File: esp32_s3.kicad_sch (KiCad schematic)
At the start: 4 parts, among them J1 uart, J2 Conn_01x02, J4 i2c, U7 ESP32-S3-DEVKITC-1-N8R2

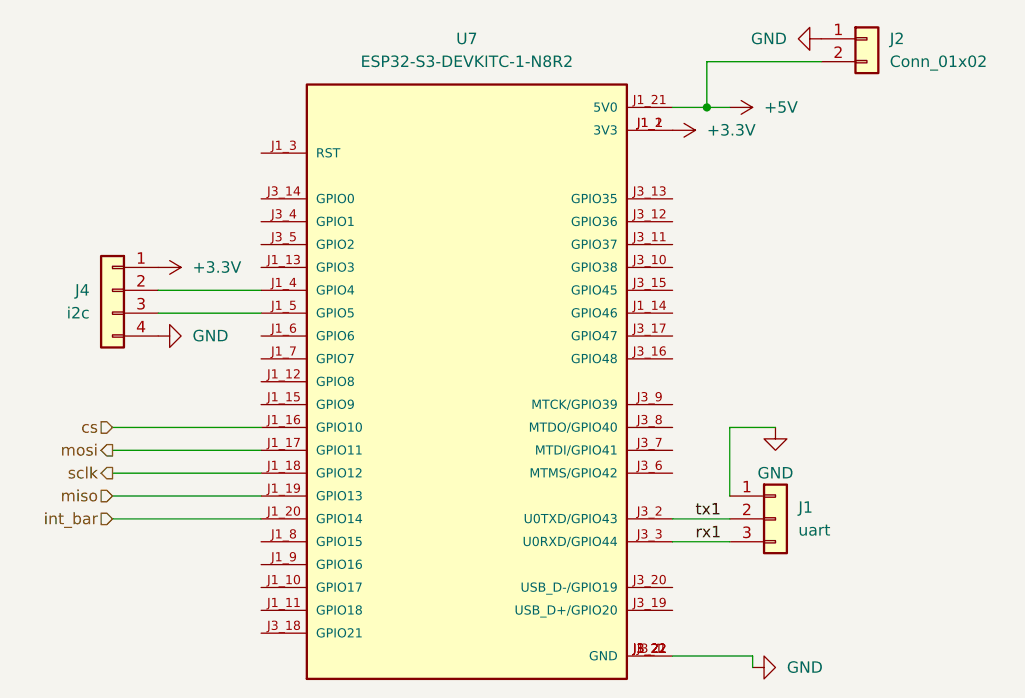
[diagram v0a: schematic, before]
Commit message: substituição do buffer de tensão com opa350 pela referencia de tensão ADR441xRZ
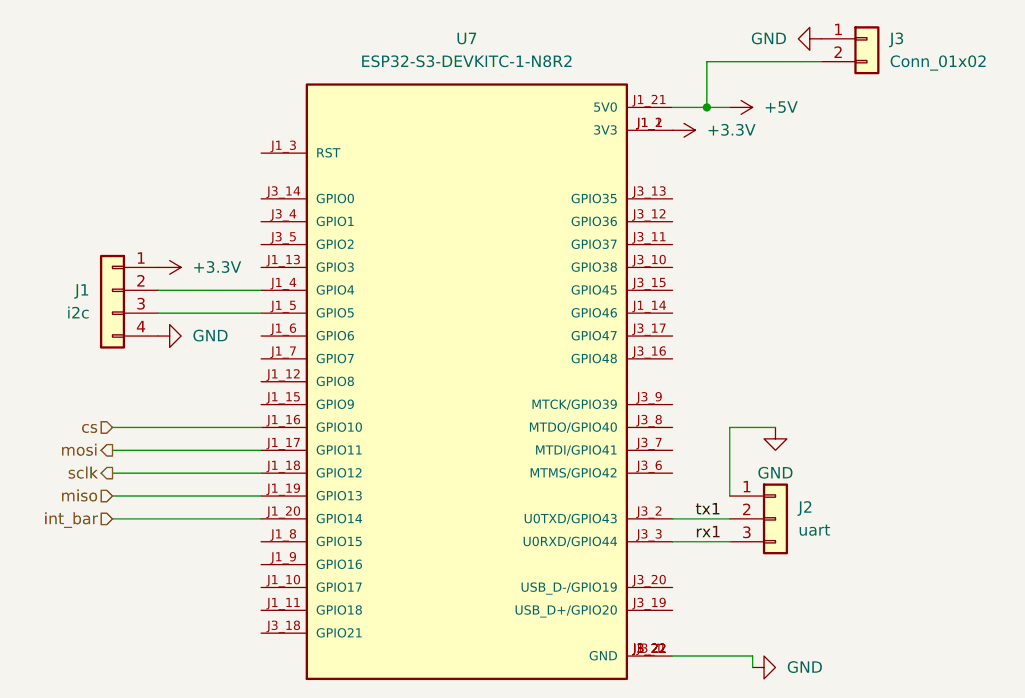
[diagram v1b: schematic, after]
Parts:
- renumbered J4 to J1, J1 to J2, J2 to J3
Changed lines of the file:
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@@
 		(on_board yes)
 		(dnp no)
-		(property "Reference" "J1"
+		(property "Reference" "J2"
 			(at 173.99 114.2999 0)
 			(effects
@@
 			(project "esp32_ads1256"
 				(path "/dbf90267-57f9-4f5a-8904-b91a6fafdaf7/fa4526fe-eebd-4bd6-aaf2-b915932153cf"
-					(reference "J1")
+					(reference "J2")
 					(unit 1)
 				)
@@
 		(dnp no)
 		(fields_autoplaced yes)
-		(property "Reference" "#PWR061"
+		(property "Reference" "#PWR058"
 			(at 170.18 62.23 0)
 			(effects
@@
 			(project "esp32_ads1256"
 				(path "/dbf90267-57f9-4f5a-8904-b91a6fafdaf7/fa4526fe-eebd-4bd6-aaf2-b915932153cf"
-					(reference "#PWR061")
+					(reference "#PWR058")
 					(unit 1)
 				)
@@
 		(dnp no)
 		(fields_autoplaced yes)
-		(property "Reference" "#PWR064"
+		(property "Reference" "#PWR053"
 			(at 109.22 95.25 0)
 			(effects
@@
 			(project "esp32_ads1256"
 				(path "/dbf90267-57f9-4f5a-8904-b91a6fafdaf7/fa4526fe-eebd-4bd6-aaf2-b915932153cf"
-					(reference "#PWR064")
+					(reference "#PWR053")
 					(unit 1)
 				)
@@
 		(dnp no)
 		(fields_autoplaced yes)
-		(property "Reference" "#PWR058"
+		(property "Reference" "#PWR055"
 			(at 162.56 69.85 0)
 			(effects
@@
 			(project "esp32_ads1256"
 				(path "/dbf90267-57f9-4f5a-8904-b91a6fafdaf7/fa4526fe-eebd-4bd6-aaf2-b915932153cf"
-					(reference "#PWR058")
+					(reference "#PWR055")
 					(unit 1)
 				)
@@
 		(on_board yes)
 		(dnp no)
-		(property "Reference" "J4"
+		(property "Reference" "J1"
 			(at 95.25 90.1699 0)
 			(effects
@@
 			(project ""
 				(path "/dbf90267-57f9-4f5a-8904-b91a6fafdaf7/fa4526fe-eebd-4bd6-aaf2-b915932153cf"
-					(reference "J4")
+					(reference "J1")
 					(unit 1)
 				)
@@
 		(dnp no)
 		(fields_autoplaced yes)
-		(property "Reference" "#PWR059"
+		(property "Reference" "#PWR057"
 			(at 171.45 111.76 0)
 			(effects
@@
 			(project "esp32_ads1256"
 				(path "/dbf90267-57f9-4f5a-8904-b91a6fafdaf7/fa4526fe-eebd-4bd6-aaf2-b915932153cf"
-					(reference "#PWR059")
+					(reference "#PWR057")
 					(unit 1)
 				)
@@
 		(dnp no)
 		(fields_autoplaced yes)
-		(property "Reference" "J2"
+		(property "Reference" "J3"
 			(at 184.15 62.2299 0)
 			(effects
@@
 			(project "esp32_ads1256"
 				(path "/dbf90267-57f9-4f5a-8904-b91a6fafdaf7/fa4526fe-eebd-4bd6-aaf2-b915932153cf"
-					(reference "J2")
+					(reference "J3")
 					(unit 1)
 				)
@@
 		(dnp no)
 		(fields_autoplaced yes)
-		(property "Reference" "#PWR062"
+		(property "Reference" "#PWR054"
 			(at 156.21 72.39 0)
 			(effects
@@
 			(project ""
 				(path "/dbf90267-57f9-4f5a-8904-b91a6fafdaf7/fa4526fe-eebd-4bd6-aaf2-b915932153cf"
-					(reference "#PWR062")
+					(reference "#PWR054")
 					(unit 1)
 				)
@@
 		(dnp no)
 		(fields_autoplaced yes)
-		(property "Reference" "#PWR063"
+		(property "Reference" "#PWR052"
 			(at 99.06 87.63 0)
 			(effects
@@
 			(project ""
 				(path "/dbf90267-57f9-4f5a-8904-b91a6fafdaf7/fa4526fe-eebd-4bd6-aaf2-b915932153cf"
-					(reference "#PWR063")
+					(reference "#PWR052")
 					(unit 1)
 				)
@@
 		(dnp no)
 		(fields_autoplaced yes)
-		(property "Reference" "#PWR060"
+		(property "Reference" "#PWR056"
 			(at 175.26 132.08 0)
 			(effects
@@
 			(project "esp32_ads1256"
 				(path "/dbf90267-57f9-4f5a-8904-b91a6fafdaf7/fa4526fe-eebd-4bd6-aaf2-b915932153cf"
-					(reference "#PWR060")
-					(unit 1)
-				)
+					(reference "#PWR056")
+					(unit 1)
+				)
